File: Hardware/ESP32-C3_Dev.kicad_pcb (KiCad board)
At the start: 2 copper layers, 32.7 x 47.2 mm, 103 parts, among them J4 USB_C_Receptacle_USB2.0_16P, J5 Conn_01x03_Socket, J6 Conn_01x03_Socket, J8 Conn_01x02_Pin, Q1 Dual_NMOS_8205A, SW1 SW_MEC_5G, SW2 SW_MEC_5G, U1 ESP32-C3-WROOM-02, U2 AMS1117-3.3, U3 DW01A, U4 TLV9002S, U5 OLED_SSD1306, U6 TP4056, U8 BMP388, U9 XC6220B181MR

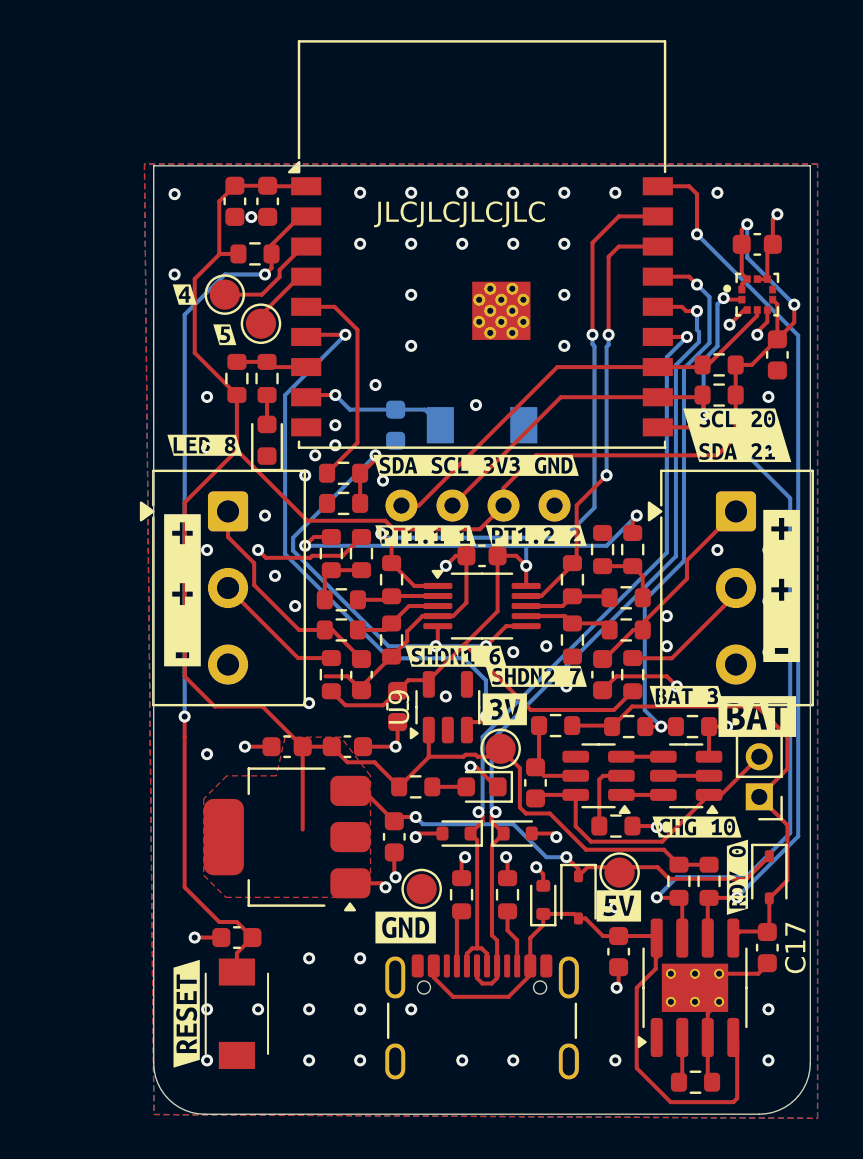
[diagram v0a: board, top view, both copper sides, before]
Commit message: wip
added screenshots, modified battery connection and silkscreen
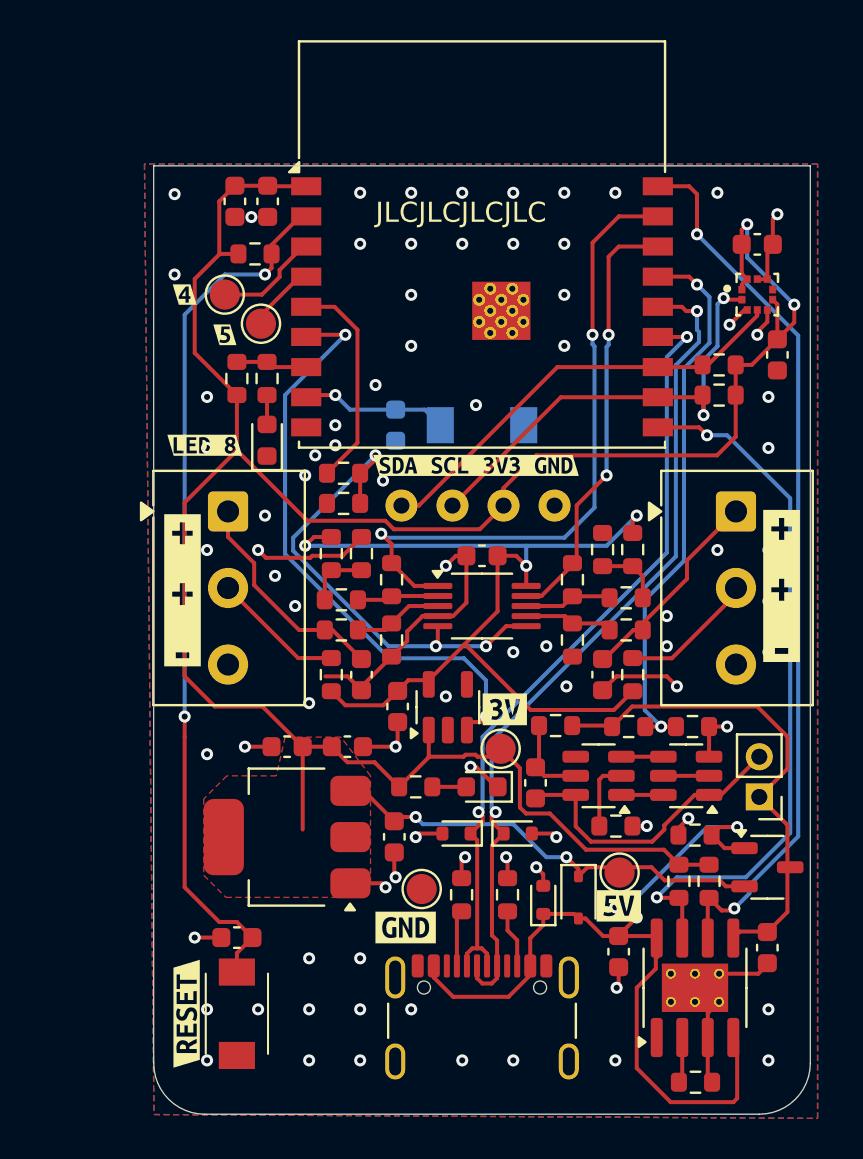
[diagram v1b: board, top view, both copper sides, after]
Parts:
- removed D8: 1N5819WS, Diode_SMD:D_SOD-323
- removed kibuzzard-68E97FD1: G***, kibuzzard-68E97FD1
- removed kibuzzard-68E97FF2: G***, kibuzzard-68E97FF2
- removed kibuzzard-68E98035: G***, kibuzzard-68E98035
- removed kibuzzard-68E98172: G***, kibuzzard-68E98172
- removed kibuzzard-68E98408: G***, kibuzzard-68E98408
- removed kibuzzard-68EE7185: G***, kibuzzard-68EE7185
- removed kibuzzard-68EE718D: G***, kibuzzard-68EE718D
- removed kibuzzard-68EE71B1: G***, kibuzzard-68EE71B1
- removed kibuzzard-68EE71C0: G***, kibuzzard-68EE71C0
- added Q2: DMG2305UX, Package_TO_SOT_SMD:SOT-23-3, F.Cu at (155.0, 93.5)
- added R32: 10K, Resistor_SMD:R_0603_1608Metric, F.Cu at (151.4, 91.9)
- added kibuzzard-68FD1544: G***, kibuzzard-68FD1544, B.Cu at (140.5, 101.0)
- kibuzzard-68E985AE: moved to B.Cu
- moved kibuzzard-68E985AE 7.07 mm to (153.5, 93.0), turned to 180 degrees
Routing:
- net USB5V: track 31.6 -> 43.7 mm, vias 0 -> 2
- net +5V: track 23.9 -> 22.3 mm
- net /Controller/READY: track 43.9 -> 44.7 mm
- net GND: track 58.0 -> 58.6 mm, vias 82 -> 83

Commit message: First Release
HW ordered at Aisler, SW wip
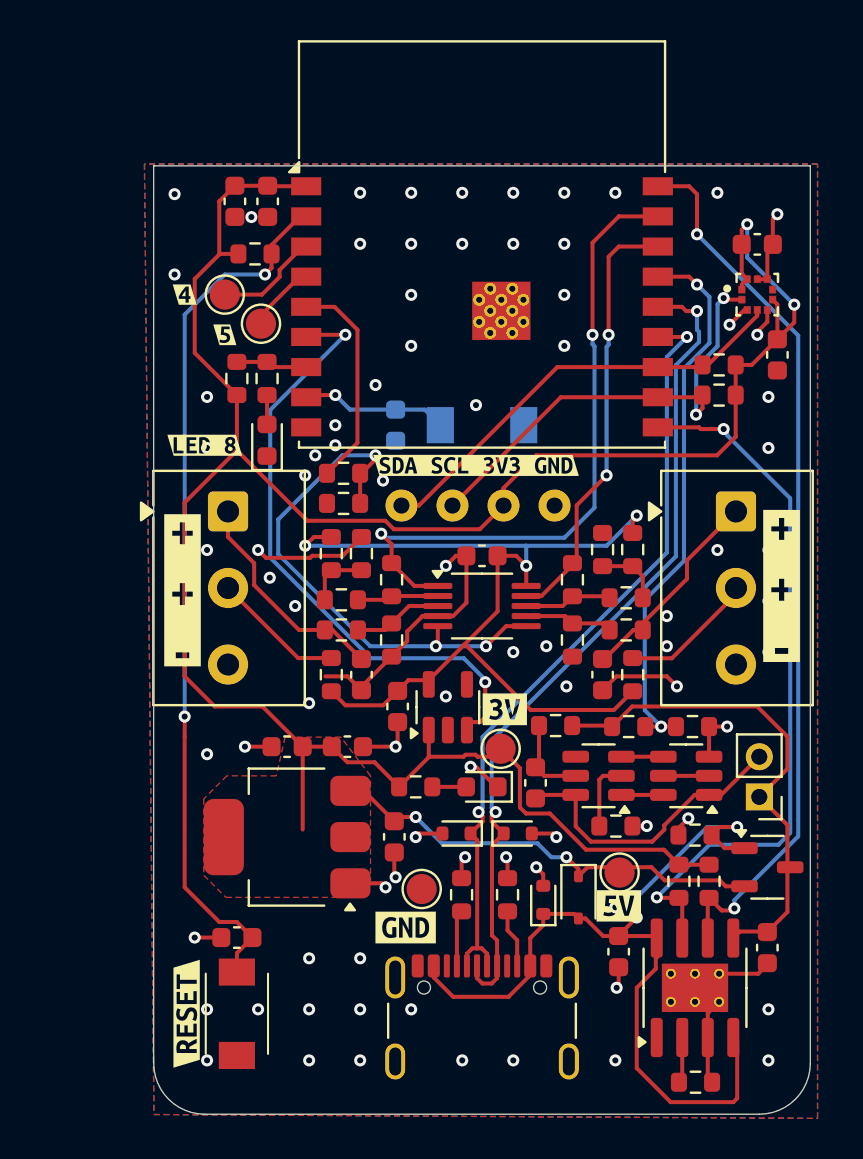
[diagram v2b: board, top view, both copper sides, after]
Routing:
- net /Controller/SHDN1: track 24.3 -> 26.4 mm
- net /Controller/SHDNLDO: track 29.6 -> 30.8 mm
- net GND: vias 83 -> 82
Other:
- board text removed: "JLCJLCJLCJLC"
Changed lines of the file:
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@@
 			(pinfunction "VO")
 			(pintype "power_out")
+			(zone_connect 2)
 		)
 		(pad "3" smd roundrect
@@
 				(font
 					(size 0.001 0.001)
+					(thickness 0.15)
 				)
 				(justify mirror)
@@
 				(font
 					(size 0.001 0.001)
+					(thickness 0.15)
 				)
 				(justify mirror)
@@
 		(layer "Edge.Cuts")
 	)
-	(gr_text "JLCJLCJLCJLC"
-		(at 135.5 61.5 0)
-		(layer "F.SilkS")
-		(effects
-			(font
-				(size 1 1)
-				(thickness 0.1)
-			)
-			(justify left bottom)
-		)
-	)
 	(dimension
 		(type orthogonal)
@@
 	)
 	(segment
-		(start 145 93)
-		(end 144 93)
+		(start 144.252 93)
+		(end 143.556295 92.304295)
 		(width 0.2)
 		(layer "B.Cu")
@@
 	)
 	(segment
-		(start 144 93)
-		(end 142.357185 91.357185)
+		(start 143.556295 92.304295)
+		(end 138.804295 92.304295)
 		(width 0.2)
 		(layer "B.Cu")
@@
 	)
 	(segment
-		(start 137.857185 91.357185)
+		(start 138.804295 92.304295)
 		(end 137.5 91)
 		(width 0.2)
@@
 	)
 	(segment
-		(start 142.357185 91.357185)
-		(end 137.857185 91.357185)
+		(start 145 93)
+		(end 144.252 93)
 		(width 0.2)
 		(layer "B.Cu")
@@
 	)
 	(via
-		(at 130 76)
-		(size 0.6)
-		(drill 0.3)
-		(layers "F.Cu" "B.Cu")
-		(free yes)
-		(net 2)
-	)
-	(via
 		(at 132.195477 98.033)
 		(size 0.6)
@@
 	)
 	(via
-		(at 130.5 79)
+		(at 130.236466 79.092)
 		(size 0.6)
 		(drill 0.3)
@@
 	)
 	(segment
-		(start 135.5 73)
-		(end 131.399 77.101)
+		(start 133.849943 73)
+		(end 135.5 73)
 		(width 0.2)
 		(layer "B.Cu")
@@
 	)
 	(segment
-		(start 136.150057 82.5)
-		(end 138.5 82.5)
+		(start 138.5 82.5)
+		(end 135.2351 82.5)
+		(width 0.2)
+		(layer "B.Cu")
+		(net 21)
+	)
+	(segment
+		(start 135.2351 82.5)
+		(end 130.660155 77.925055)
 		(width 0.2)
 		(layer "B.Cu")
@@
 	)
 	(segment
-		(start 131.399 77.748943)
-		(end 136.150057 82.5)
+		(start 130.660155 77.925055)
+		(end 130.660155 76.189788)
 		(width 0.2)
 		(layer "B.Cu")
@@
 	)
 	(segment
-		(start 131.399 77.101)
-		(end 131.399 77.748943)
+		(start 130.660155 76.189788)
+		(end 133.849943 73)
 		(width 0.2)
 		(layer "B.Cu")
@@
 	)
 	(segment
+		(start 151.775 70)
+		(end 151.775 70.651825)
+		(width 0.2)
+		(layer "F.Cu")
+		(net 23)
+	)
+	(segment
 		(start 151.825735 70.158735)
 		(end 151.775 70.108)
@@
 	)
 	(segment
+		(start 151.775 70.651825)
+		(end 151.451001 70.975824)
+		(width 0.2)
+		(layer "F.Cu")
+		(net 23)
+	)
+	(segment
 		(start 152.825735 65.174265)
 		(end 152.90147 65.25)
@@
 		(net 23)
 	)
-	(segment
-		(start 151.825735 71)
-		(end 151.825735 70.158735)
-		(width 0.2)
-		(layer "F.Cu")
-		(net 23)
-	)
 	(via
 		(at 152.825735 65.174265)
@@
 	)
 	(via
-		(at 151.825735 71)
+		(at 151.451001 70.975824)
 		(size 0.6)
 		(drill 0.3)
@@
 	)
 	(segment
-		(start 152.521493 65.478507)
-		(end 152.825735 65.174265)
+		(start 151.46 68.632143)
+		(end 152.521493 67.57065)
 		(width 0.2)
 		(layer "B.Cu")
@@
 	)
 	(segment
-		(start 151.825735 68.266408)
-		(end 152.521493 67.57065)
+		(start 152.521493 67.57065)
+		(end 152.521493 65.478507)
 		(width 0.2)
 		(layer "B.Cu")
@@
 	)
 	(segment
-		(start 152.521493 67.57065)
-		(end 152.521493 65.478507)
+		(start 152.521493 65.478507)
+		(end 152.825735 65.174265)
 		(width 0.2)
 		(layer "B.Cu")
@@
 	)
 	(segment
-		(start 151.825735 71)
-		(end 151.825735 68.266408)
+		(start 151.451001 70.975824)
+		(end 151.46 70.966825)
+		(width 0.2)
+		(layer "B.Cu")
+		(net 23)
+	)
+	(segment
+		(start 151.46 70.966825)
+		(end 151.46 68.632143)
 		(width 0.2)
 		(layer "B.Cu")
@@
 	)
 	(segment
-		(start 149.525 95.025)
-		(end 149.5 95)
+		(start 151.692164 71.692164)
+		(end 151.608 71.608)
 		(width 0.2)
 		(layer "F.Cu")
@@
 	)
 	(segment
-		(start 149.55 71.608)
-		(end 151.608 71.608)
+		(start 149.525 95.025)
+		(end 149.5 95)
 		(width 0.2)
 		(layer "F.Cu")
@@
 	)
 	(segment
-		(start 151.608 71.608)
-		(end 152 72)
+		(start 152.825 71.692164)
+		(end 151.692164 71.692164)
 		(width 0.2)
 		(layer "F.Cu")
@@
 		(net 32)
 	)
+	(segment
+		(start 151.608 71.608)
+		(end 149.55 71.608)
+		(width 0.2)
+		(layer "F.Cu")
+		(net 32)
+	)
 	(via
 		(at 149.5 95)
@@
 	)
 	(via
-		(at 152 72)
+		(at 152.825 71.692164)
 		(size 0.6)
 		(drill 0.3)
@@
 	)
 	(segment
-		(start 152 72)
+		(start 153 71.867164)
 		(end 153 72)
 		(width 0.2)
@@
 	)
 	(segment
+		(start 152.825 71.692164)
+		(end 153 71.867164)
+		(width 0.2)
+		(layer "B.Cu")
+		(net 32)
+	)
+	(segment
 		(start 156.138 91.7949)
-		(end 153.9329 94)
+		(end 155.55045 92.38245)
 		(width 0.2)
 		(layer "B.Cu")
@@
 	)
 	(segment
-		(start 156.138 75.138)
-		(end 156.138 91.7949)
+		(start 152.11755 92.38245)
+		(end 149.5 95)
 		(width 0.2)
 		(layer "B.Cu")
@@
 	)
 	(segment
-		(start 153.9329 94)
-		(end 150.5 94)
+		(start 156.138 75.138)
+		(end 156.138 91.7949)
 		(width 0.2)
 		(layer "B.Cu")
@@
 	)
 	(segment
-		(start 150.5 94)
-		(end 149.5 95)
+		(start 155.55045 92.38245)
+		(end 152.11755 92.38245)
 		(width 0.2)
 		(layer "B.Cu")
@@
 	)
 	(segment
-		(start 154.107875 94.801566)
-		(end 154.107875 94.392125)
-		(width 0.2)
-		(layer "B.Cu")
-		(net 40)
-	)
-	(segment
 		(start 153.359441 95.55)
-		(end 154.107875 94.801566)
+		(end 153.359441 95.140559)
 		(width 0.2)
 		(layer "B.Cu")
@@
 	)
 	(segment
-		(start 156.539 91.961)
-		(end 156.539 67.039)
+		(start 153.359441 95.140559)
+		(end 156.539 91.961)
 		(width 0.2)
 		(layer "B.Cu")
@@
 	)
 	(segment
-		(start 154.107875 94.392125)
-		(end 156.539 91.961)
+		(start 156.539 67.039)
+		(end 151.5 62)
 		(width 0.2)
 		(layer "B.Cu")
@@
 	)
 	(segment
-		(start 156.539 67.039)
-		(end 151.5 62)
+		(start 156.539 91.961)
+		(end 156.539 67.039)
 		(width 0.2)
 		(layer "B.Cu")
@@
 	)
 	(segment
+		(start 140.717372 86.275)
+		(end 140.96 86.032372)
+		(width 0.2)
+		(layer "F.Cu")
+		(net 48)
+	)
+	(segment
 		(start 140.05 86.275)
 		(end 140.717372 86.275)
@@
 	)
 	(segment
-		(start 140.717372 86.275)
-		(end 140.996186 85.996186)
+		(start 132.158 67)
+		(end 132.05 67.108)
 		(width 0.2)
 		(layer "F.Cu")
@@
 	)
 	(segment
-		(start 132.158 67)
-		(end 132.05 67.108)
+		(start 140.96 86.032372)
+		(end 140.96 84.292)
 		(width 0.2)
 		(layer "F.Cu")
@@
 	)
 	(via
-		(at 140.996186 85.996186)
+		(at 140.96 84.292)
 		(size 0.6)
 		(drill 0.3)
@@
 	)
 	(segment
-		(start 130.998 70.002)
-		(end 134 67)
+		(start 139.899 83.101)
+		(end 140.96 84.162)
 		(width 0.2)
 		(layer "B.Cu")
@@
 	)
 	(segment
-		(start 139.899 83.101)
-		(end 136.183957 83.101)
+		(start 135.269 83.101)
+		(end 139.899 83.101)
 		(width 0.2)
 		(layer "B.Cu")
@@
 	)
 	(segment
-		(start 136.183957 83.101)
-		(end 130.998 77.915043)
+		(start 134 67)
+		(end 130.259155 70.740845)
 		(width 0.2)
 		(layer "B.Cu")
@@
 	)
 	(segment
-		(start 140.996186 85.996186)
-		(end 141 85.992372)
+		(start 140.996186 84.198186)
+		(end 140.96 84.162)
 		(width 0.2)
 		(layer "B.Cu")
@@
 	)
 	(segment
-		(start 140.996186 84.198186)
-		(end 139.899 83.101)
+		(start 130.259155 78.091155)
+		(end 135.269 83.101)
 		(width 0.2)
 		(layer "B.Cu")
@@
 	)
 	(segment
-		(start 140.996186 85.996186)
-		(end 140.996186 84.198186)
+		(start 130.259155 70.740845)
+		(end 130.259155 78.091155)
 		(width 0.2)
 		(layer "B.Cu")
@@
 	)
 	(segment
-		(start 130.998 77.915043)
-		(end 130.998 70.002)
+		(start 140.96 84.292)
+		(end 140.96 84.162)
 		(width 0.2)
 		(layer "B.Cu")

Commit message: adding buck-boost
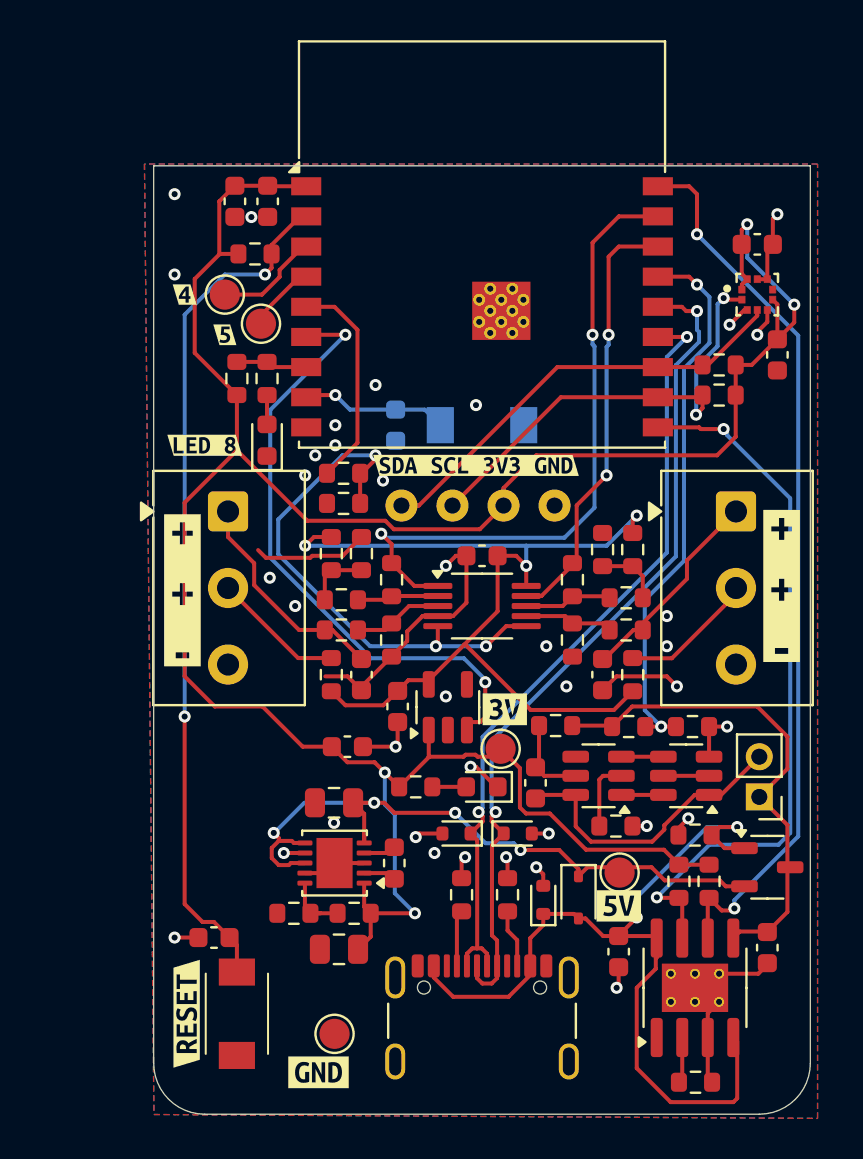
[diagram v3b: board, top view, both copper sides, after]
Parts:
- removed C1, C2: 10u 10V, Capacitor_SMD:C_0603_1608Metric
- added C13: 20u 10V, Capacitor_SMD:C_0805_2012Metric, F.Cu at (133.4, 90.3)
- added C18: 20u 10V, Capacitor_SMD:C_0805_2012Metric, F.Cu at (133.7, 97.6)
- added L1: 2u2, Inductor_SMD:L_0603_1608Metric, F.Cu at (136.4, 93.3)
- added R33: 470K, Resistor_SMD:R_0603_1608Metric, F.Cu at (134.4, 95.8)
- added R34: 82K, Resistor_SMD:R_0603_1608Metric, F.Cu at (131.4, 95.8)
- U2: value AMS1117-3.3 -> RT6150A; footprint Package_TO_SOT_SMD:SOT-223-3_TabPin2 -> Package_DFN_QFN:WDFN-10-1EP_3x3mm_P0.5mm_EP1.8x2.5mm
- moved TP3 8.41 mm to (133.5, 101.8)
- moved kibuzzard-68E986EB 8.41 mm to (132.7, 103.7)
- moved U2 2.69 mm to (133.5, 93.3)
- moved C8 1.14 mm to (127.5, 97.0)
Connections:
- U2 pad 1: GND -> +3.3V
- U2 pad 2: +3.3V -> Net-(U2-LX2)
- U2 pad 3: +5V -> GND
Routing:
- net +5V: track 22.3 -> 34.8 mm, vias 2 -> 4
- net +3.3V: track 118.3 -> 127.7 mm, vias 2 -> 4
- net Net-(U2-FB): track 0.00 -> 3.46 mm
- net Net-(U2-LX1): track 0.00 -> 1.62 mm
- net Net-(U2-LX2): track 0.00 -> 1.62 mm
- net GND: track 58.6 -> 57.0 mm, vias 82 -> 36
- net /Power Supply/PS: track 0.00 -> 1.05 mm, vias 0 -> 1
- net /Controller/EN: track 43.7 -> 42.9 mm
- removed copper zone on F.Cu, net +3.3V

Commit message: V2 fertig gestellt!
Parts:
- removed J5, J6: Conn_01x03_Socket, TerminalBlock_Phoenix:TerminalBlock_Phoenix_MKDS-1-3-3.81_1x03_P3.81mm_Horizontal
- removed R18, R19: 10K, Resistor_SMD:R_0603_1608Metric
- removed kibuzzard-68E98378 (x2): G***, kibuzzard-68E98378
- removed kibuzzard-68E9858B: G***, kibuzzard-68E9858B
- removed kibuzzard-68EE7E42: G***, kibuzzard-68EE7E42
- removed kibuzzard-68EE7E4D: G***, kibuzzard-68EE7E4D
- removed kibuzzard-68FD1544: G***, kibuzzard-68FD1544
- added C1: 10n, Capacitor_SMD:C_0603_1608Metric, F.Cu at (152.0, 61.3)
- added C2: 10n, Capacitor_SMD:C_0603_1608Metric, F.Cu at (152.0, 62.8)
- added J1: Conn_01x02_Socket, _PS_LIB_PCB:TerminalBlock_Phoenix_MKDS-1-2-3.81_1x02_P3.81mm_Horizontal, F.Cu at (128.0, 78.0)
- added J2: Conn_01x02_Socket, _PS_LIB_PCB:TerminalBlock_Phoenix_MKDS-1-2-3.81_1x02_P3.81mm_Horizontal, F.Cu at (153.4, 81.8)
- added R35: PT100, Resistor_SMD:R_0805_2012Metric, F.Cu at (130.5, 79.8)
- added kibuzzard-6930773F: G***, kibuzzard-6930773F, B.Cu at (140.5, 101.0)
- added kibuzzard-69307756: G***, kibuzzard-69307756, B.Cu at (151.5, 89.0)
- J8: footprint Connector_PinHeader_2.00mm:PinHeader_1x02_P2.00mm_Vertical -> Connector_JST:JST_PH_B2B-PH-K_1x02_P2.00mm_Vertical
- R16: value 10K -> 3K9
- moved kibuzzard-68E986B5 12.2 mm to (130.0, 87.8)
- moved TP4 11.9 mm to (130.0, 85.8)
- moved kibuzzard-68E97F46 3.35 mm to (140.5, 72.3)
- moved C7 1.80 mm to (136.5, 69.7)
- moved SW1 1.80 mm to (140.8, 69.7)
- moved R32 1.64 mm to (150.6, 93.3)
- moved Q1 0.80 mm to (150.2, 89.0)
- moved Q2 0.76 mm to (154.3, 93.8)
- moved J8 0.72 mm to (153.9, 89.8), turned to 90 degrees
- moved R20 0.60 mm to (147.5, 86.5)
- moved R21 0.60 mm to (150.7, 86.5)
- moved U3 0.60 mm to (146.0, 89.0)
- moved C9 0.59 mm to (143.2, 88.8)
- moved C15 0.46 mm to (155.0, 62.5)
- moved R8 0.30 mm to (147.2, 91.5)
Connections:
- C11 pad 1: Net-(J5-Pin_1) -> Net-(J1-Pin_2)
- C12 pad 1: Net-(J6-Pin_1) -> Net-(J2-Pin_1)
- J8 pad 1: /Power Supply/battery+ -> /Power Supply/battery-
- J8 pad 2: /Power Supply/battery- -> /Power Supply/battery+
- R14 pad 1: Net-(J6-Pin_1) -> Net-(J2-Pin_1)
- R24 pad 2: Net-(J6-Pin_2) -> Net-(J2-Pin_1)
- R27 pad 2: Net-(J5-Pin_2) -> Net-(J1-Pin_2)
- R9 pad 1: Net-(J5-Pin_1) -> Net-(J1-Pin_2)
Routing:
- net GND: track 57.0 -> 36.6 mm, vias 36 -> 39
- net +3.3V: track 127.7 -> 110.1 mm
- net Net-(J5-Pin_1): track 11.1 -> 0.00 mm
- net Net-(J6-Pin_1): track 10.4 -> 0.00 mm
- net Net-(J2-Pin_1): track 0.00 -> 9.09 mm
- net Net-(J1-Pin_2): track 0.00 -> 8.85 mm
- net Net-(J6-Pin_2): track 6.77 -> 0.00 mm
- net Net-(J5-Pin_2): track 6.58 -> 0.00 mm
- net /Controller/CHARGING: track 35.9 -> 33.3 mm
- net /Controller/PT100_2: track 21.7 -> 23.4 mm
- net /Controller/PT100_1: track 32.8 -> 34.5 mm
- net USB5V: track 43.7 -> 42.6 mm
- net /Power Supply/battery+: track 24.9 -> 25.8 mm
- net /Controller/READY: track 44.7 -> 43.8 mm
- net /Power Supply/battery-: track 15.0 -> 14.4 mm

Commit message: housing created
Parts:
- removed C14: 100n, Capacitor_SMD:C_0603_1608Metric
- removed U9: XC6220B181MR, Package_TO_SOT_SMD:SOT-23-5
- added TP6: TestPoint, TestPoint:TestPoint_Pad_D1.5mm, F.Cu at (120.5, 72.8)
- moved R21 0.50 mm to (150.2, 86.5)
- moved R13 0.40 mm to (147.6, 80.1)
- moved R14 0.40 mm to (147.6, 81.7)
- moved R20 0.40 mm to (147.1, 86.5)
- moved R7 0.40 mm to (144.1, 86.5)
- moved J8 0.20 mm to (153.9, 89.6)
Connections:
- C10 pad 1: +1.8V -> +3.3V
- R24 pad 1: +1.8V -> +3.3V
- R26 pad 1: +1.8V -> +3.3V
- R27 pad 1: +1.8V -> +3.3V
- R28 pad 1: +1.8V -> +3.3V
- U1 pad 6: /Controller/SHDNLDO -> Net-(U1-IO7)
- U4 pad 10: +1.8V -> +3.3V
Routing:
- net +1.8V: track 47.0 -> 0.00 mm, vias 3 -> 0
- net +3.3V: track 110.1 -> 153.5 mm, vias 4 -> 7
- net /Controller/SHDNLDO: track 30.8 -> 0.00 mm, vias 2 -> 0
- net GND: track 36.6 -> 35.5 mm
- net Net-(J2-Pin_1): track 9.09 -> 8.59 mm
- net Net-(U2-FB): track 3.46 -> 2.96 mm
- net +5V: track 34.9 -> 34.4 mm
